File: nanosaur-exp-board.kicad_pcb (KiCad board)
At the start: 2 copper layers, 4 parts, among them J1 jetson_nano, J2 Screw_Terminal_01x02, J3 nanosaur_exp, SW1 SW_DPDT_x2

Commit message: Fix layout board
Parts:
- added REF**: MountingHole_2.2mm_M2, MountingHole:MountingHole_2.2mm_M2, F.Cu at (181.6, 86.4)
- added REF**: MountingHole_2.2mm_M2, MountingHole:MountingHole_2.2mm_M2, F.Cu at (181.6, 101.6)
- added REF**: MountingHole_2.2mm_M2, MountingHole:MountingHole_2.2mm_M2, F.Cu at (106.7, 101.6)
- added REF**: MountingHole_2.2mm_M2, MountingHole:MountingHole_2.2mm_M2, F.Cu at (106.7, 86.4)
- J1: footprint Connector_PinHeader_2.54mm:PinHeader_2x20_P2.54mm_Vertical -> Connector_PinSocket_2.54mm:PinSocket_2x21_P2.54mm_Vertical; moved to B.Cu
- J2: footprint TerminalBlock:TerminalBlock_Altech_AK300-2_P5.00mm -> TerminalBlock_4Ucon:TerminalBlock_4Ucon_1x02_P3.50mm_Horizontal; moved to B.Cu
- J3, SW1: moved to B.Cu
- moved SW1 45.8 mm to (167.6, 88.9), turned to 0 degrees
- moved J1 30.5 mm to (166.4, 99.1), turned to 90 degrees
- moved J2 29.6 mm to (160.0, 93.7), turned to 90 degrees
- moved J3 27.9 mm to (152.4, 87.6), turned to 90 degrees
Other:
- board outline added: 80 x 20.3 mm

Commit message: Exp improvements
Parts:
- removed REF** (x4): MountingHole_2.2mm_M2, MountingHole:MountingHole_2.2mm_M2
- added H1: MountingHole, MountingHole:MountingHole_2.1mm, F.Cu at (106.7, 86.4)
- added H2: MountingHole, MountingHole:MountingHole_2.1mm, F.Cu at (106.7, 101.6)
- added H3: MountingHole, MountingHole:MountingHole_2.1mm, F.Cu at (181.6, 101.6)
- added H4: MountingHole, MountingHole:MountingHole_2.1mm, F.Cu at (181.6, 86.4)
- SW1: footprint Button_Switch_THT:SW_CuK_JS202011AQN_DPDT_Angled -> Button_Switch_THT:SW_E-Switch_EG1271_DPDT
- moved J1 1.80 mm to (165.1, 97.8)
- moved SW1 0.66 mm to (167.6, 89.6)

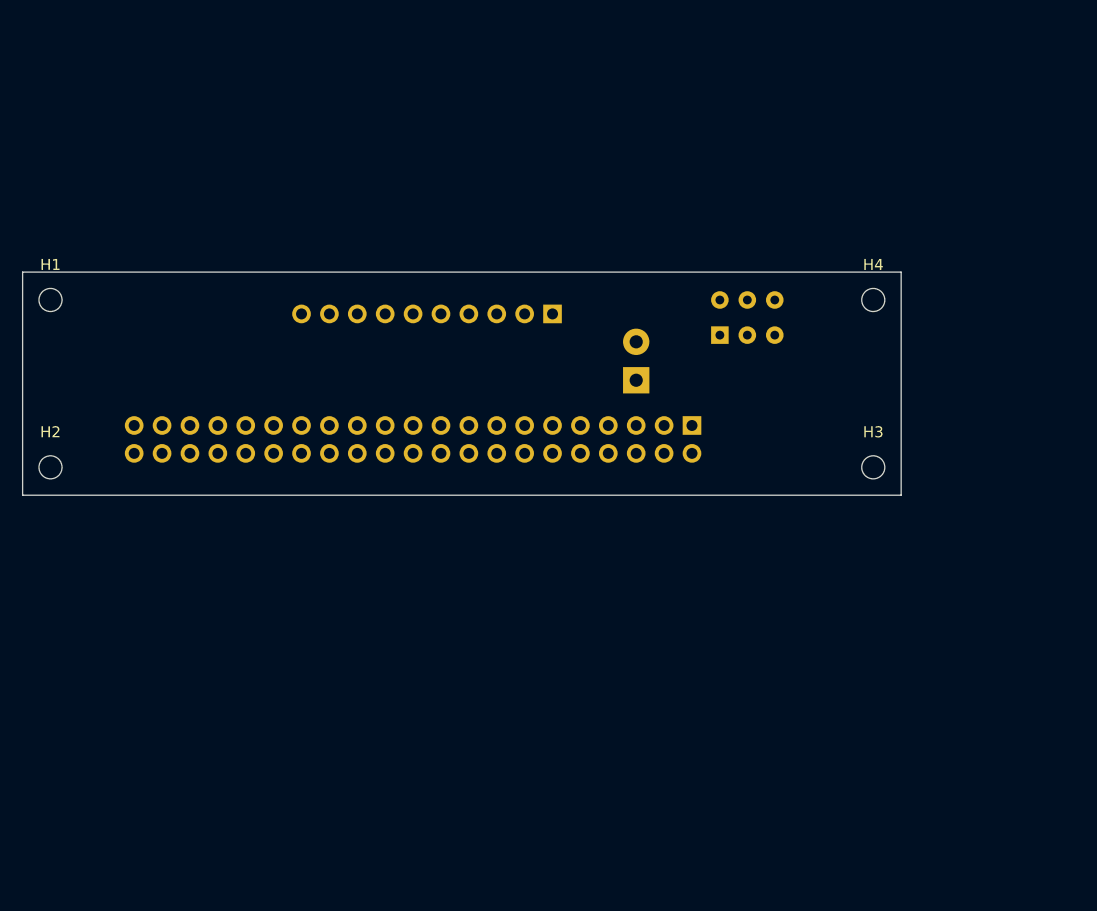
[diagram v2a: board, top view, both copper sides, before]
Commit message: Rework of schematic
I reworked the schematic and added adapters so the Users has less to solder.  Please note that these changes are currently only in the schematic not the PCB side of things. These changes will ba added soon.

Signed off by: Thore Krug
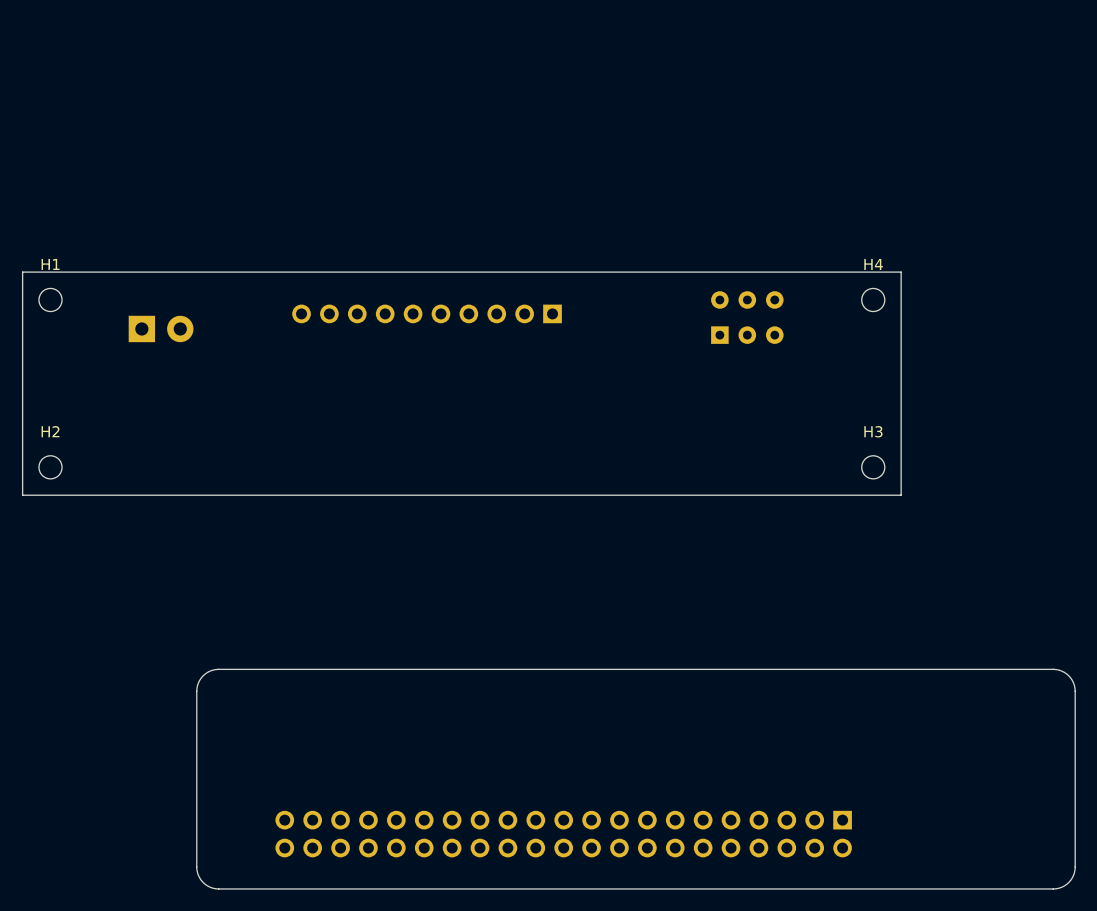
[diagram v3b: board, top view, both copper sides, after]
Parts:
- moved J2 45.3 mm to (115.0, 89.0), turned to 0 degrees
- moved J1 38.5 mm to (178.8, 133.7)
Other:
- board size 80 x 20.3 mm -> 95.9 x 56.2 mm
